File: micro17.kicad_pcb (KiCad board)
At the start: 4 copper layers, 20 x 30 mm, 94 parts, among them J1 Conn_01x05, J2 AXK640347YG, J4 USB_B_Micro, U1 STM32G473CCUx, U2 XC6220B331MR, U3 CPC1117N, U4 MCP6002, U5 MCP4451-503-ST, U6 MCP6002, U7 MCP6002, Y1 8 MHz

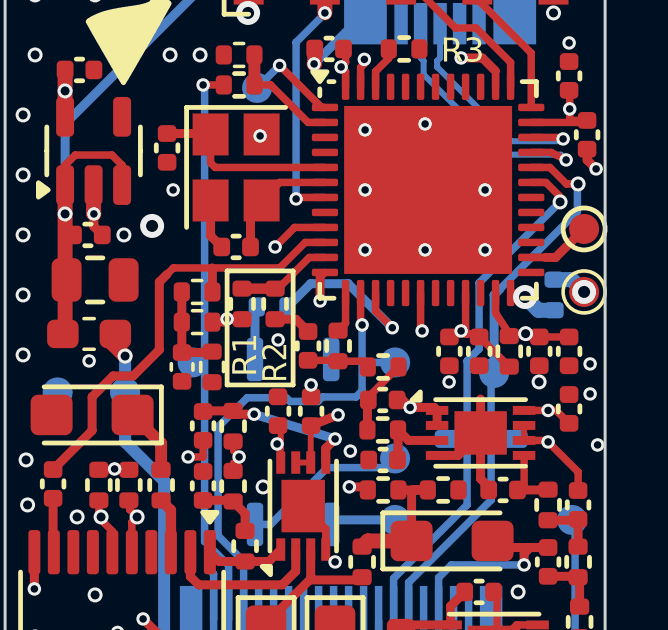
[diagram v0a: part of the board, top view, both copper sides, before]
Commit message: VREF+ connected to VDDA
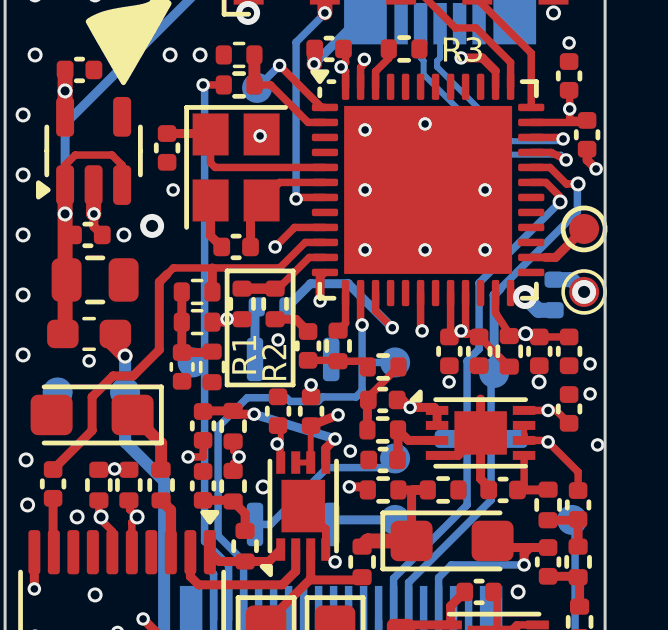
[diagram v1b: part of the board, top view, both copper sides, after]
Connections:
- U1 pad 20: unconnected-(U1-VREF+-Pad20) -> VDDA
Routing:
- net VDDA: track 19.7 -> 21.2 mm
